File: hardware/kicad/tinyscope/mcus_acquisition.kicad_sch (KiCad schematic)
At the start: 30 parts, among them J5 STM32H743, Q2 NMOS, SW1 SW_SPST, U12 STM32H743VITx, X1 25MHz, X2 32k768

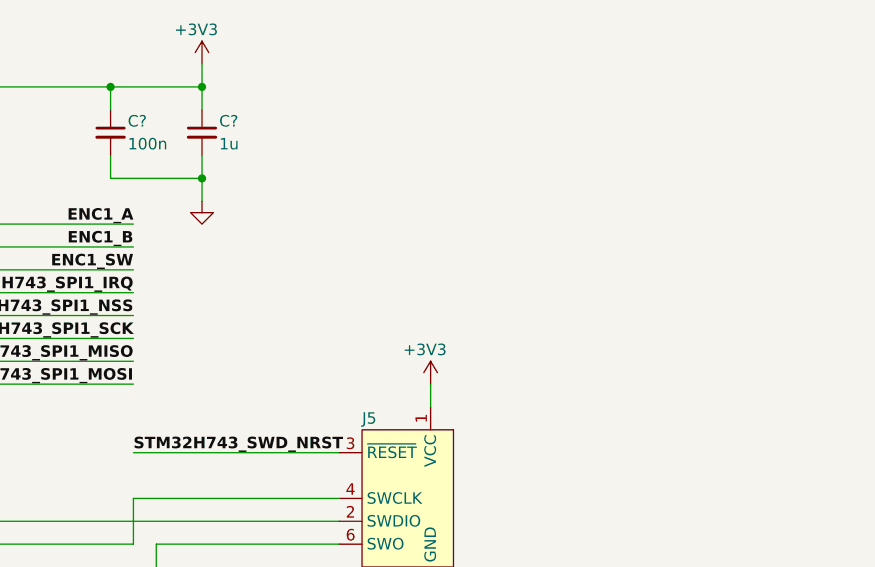
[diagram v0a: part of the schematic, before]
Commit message: feat: hardware: note: The SPI1 has to be changed due to the fact that PA4 is used by DAC1_OUT
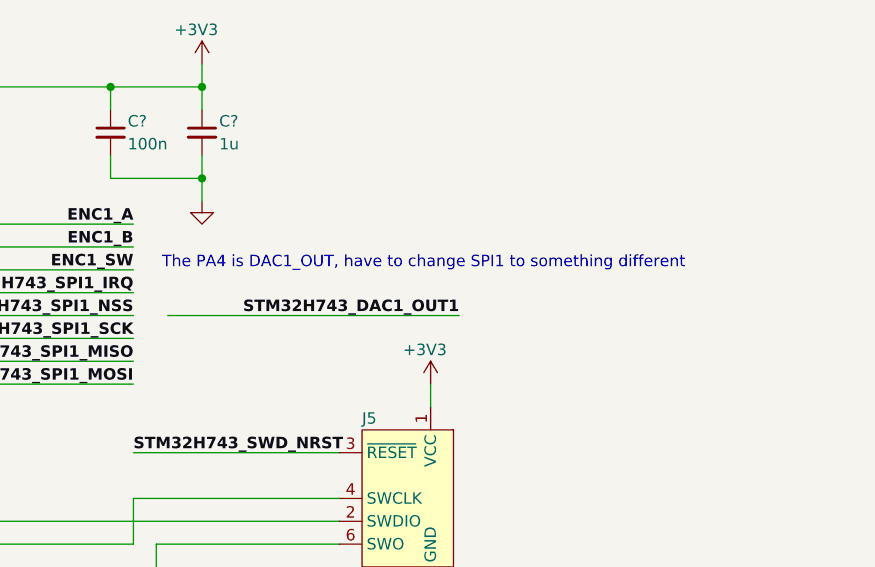
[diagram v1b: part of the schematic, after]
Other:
- note added: "The PA4 is DAC1_OUT, have to change SPI1 to something different"
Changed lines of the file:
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@@
+    (stroke (width 0) (type default))
+  )
+  (wire (pts (xy 204.47 45.72) (xy 236.855 45.72))
     (stroke (width 0) (type default))
   )
@@
     (effects (font (size 1.27 1.27)) (justify left top))
   )
+  (text "The PA4 is DAC1_OUT, have to change SPI1 to something different"
+    (at 203.835 40.64 0)
+    (effects (font (size 1.27 1.27)) (justify left bottom))
+  )
   (label "STM32H743_SPI1_SCK" (at 200.66 48.26 180) (fields_autoplaced)
     (effects (font (size 1.27 1.27) bold) (justify right bottom))
@@
     (effects (font (size 1.27 1.27) bold) (justify right bottom))
   )
+  (label "STM32H743_DAC1_OUT1" (at 236.855 45.72 180) (fields_autoplaced)
+    (effects (font (size 1.27 1.27) bold) (justify right bottom))
+  )

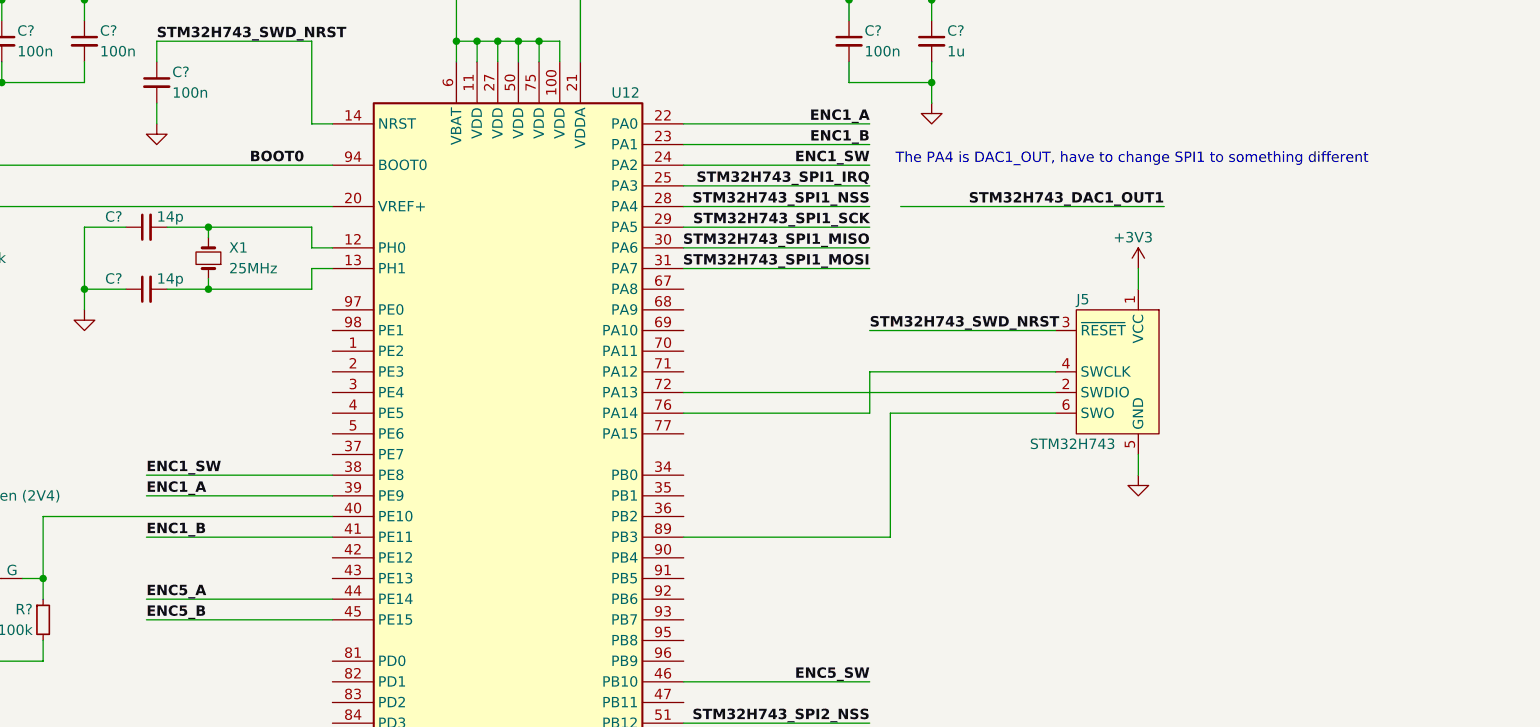
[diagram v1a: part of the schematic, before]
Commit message: feat: hardware: Switches SPI1 to SPI4. Adds DAC1_OUT1 and DAC1_OUT2
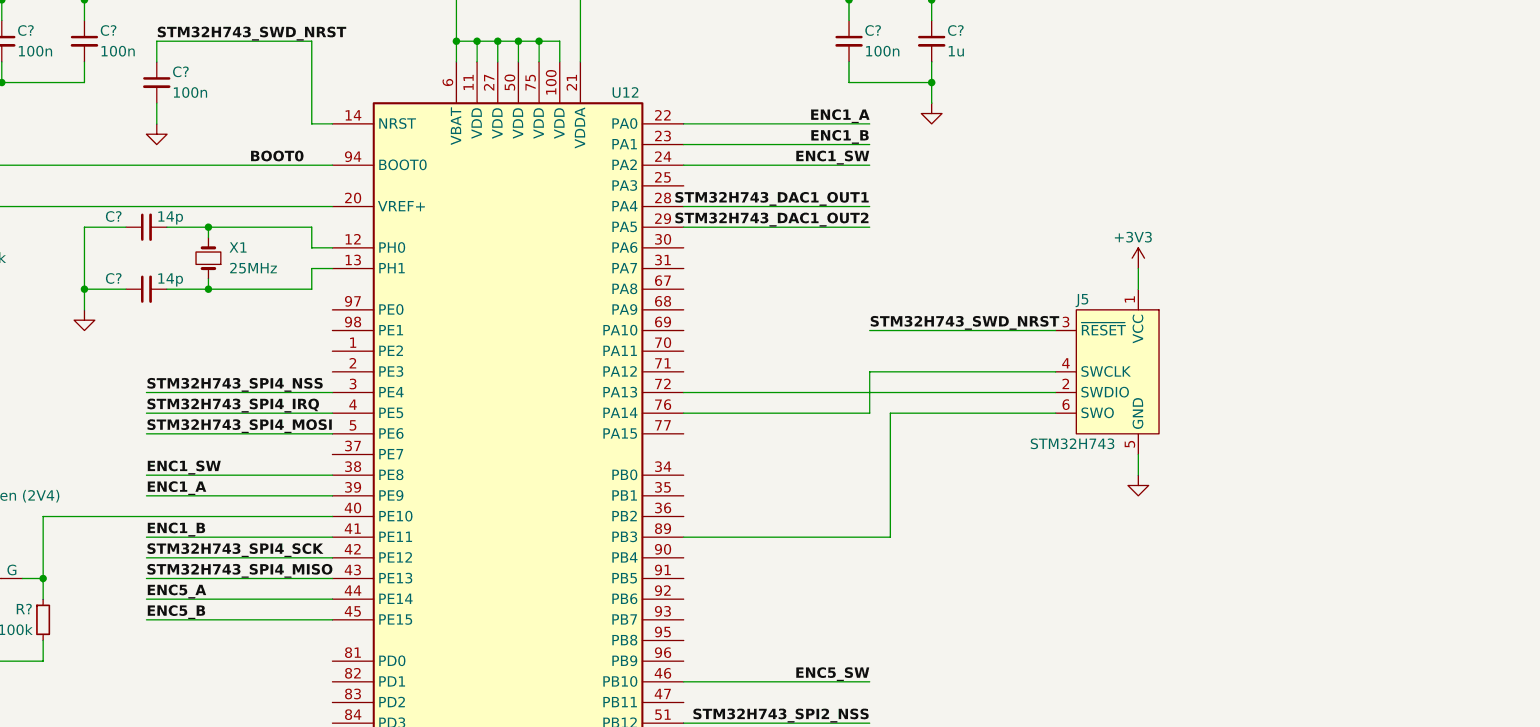
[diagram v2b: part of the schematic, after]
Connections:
- net STM32H743_SPI1_NSS is gone; now on net STM32H743_DAC1_OUT1: U12.28 (PA4)
- net STM32H743_SPI4_NSS: now reaches U12.3 (PE4)
- net STM32H743_SPI4_IRQ: now reaches U12.4 (PE5)
- net STM32H743_SPI4_SCK: now reaches U12.42 (PE12)
- net STM32H743_SPI4_MISO: now reaches U12.43 (PE13)
- net STM32H743_SPI4_MOSI: now reaches U12.5 (PE6)
- net STM32H743_SPI1_IRQ: no longer names the net of U12.25 (PA3)
- net STM32H743_SPI1_MISO: no longer names the net of U12.30 (PA6)
- net STM32H743_SPI1_MOSI: no longer names the net of U12.31 (PA7)
- net STM32H743_SPI1_SCK renamed STM32H743_DAC1_OUT2
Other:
- note removed: "The PA4 is DAC1_OUT, have to change SPI1 to something different"
